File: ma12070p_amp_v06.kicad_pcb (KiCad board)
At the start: 2 copper layers, 100.4 x 80.4 mm, 83 parts, among them U1 MAX16956, U2 MA12070P

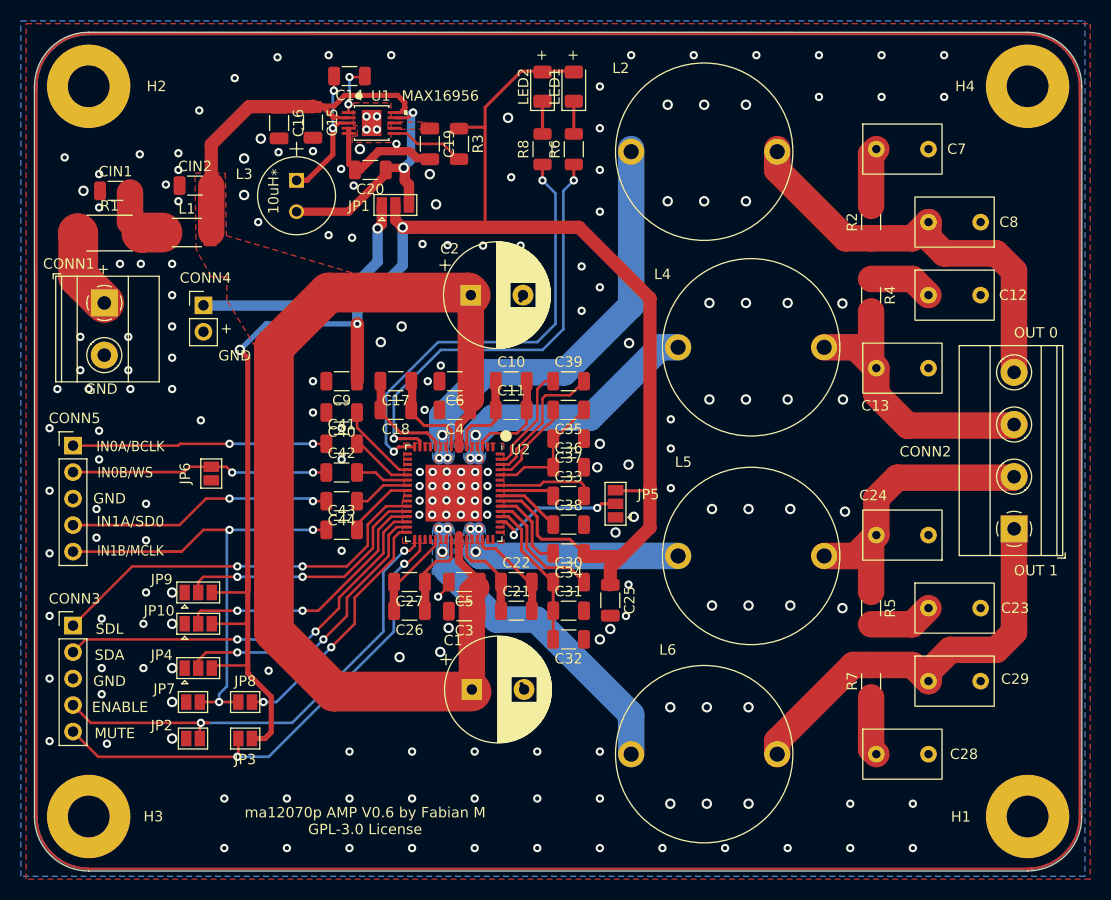
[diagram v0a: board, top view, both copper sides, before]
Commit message: redo of DRC because of mistake
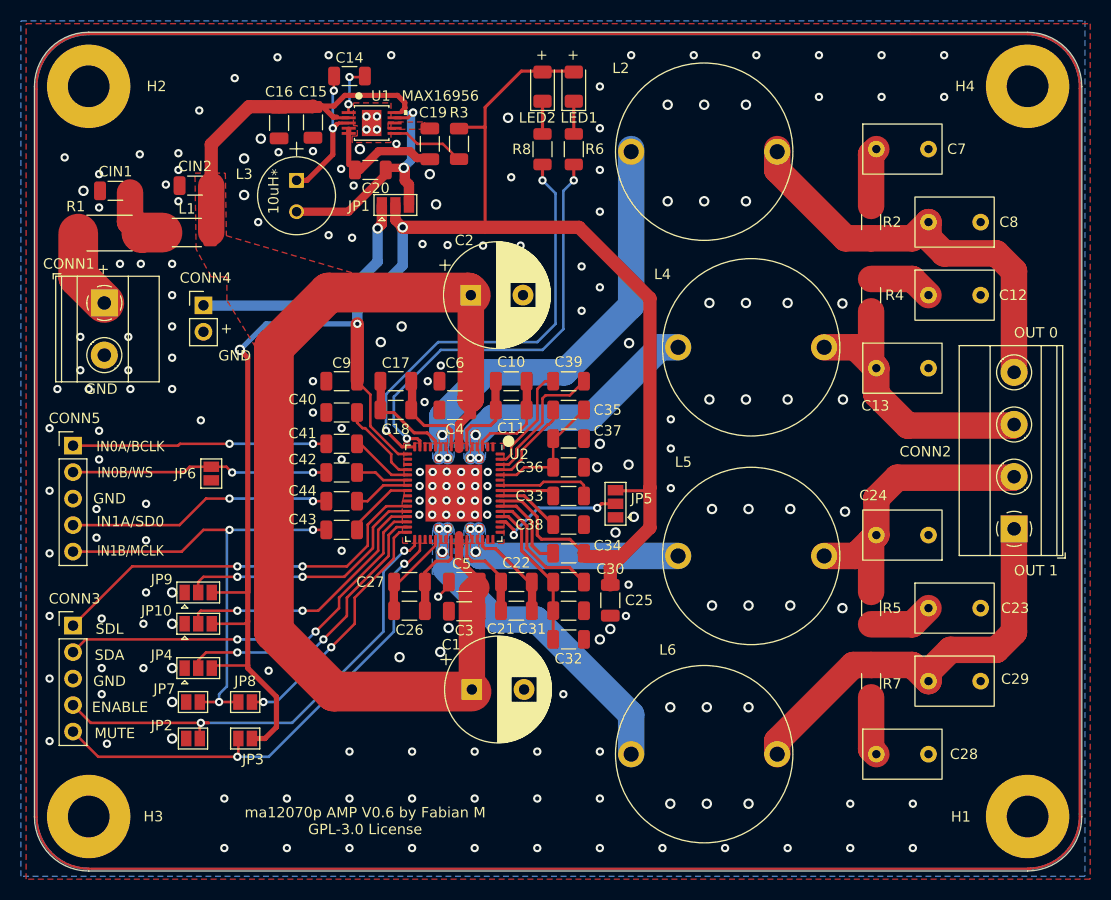
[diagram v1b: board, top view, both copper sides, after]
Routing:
- net VDD: track 185.7 -> 190.7 mm
- net Net-(C43-Pad1): track 47.7 -> 45.8 mm
- net ERR: track 42.3 -> 41.1 mm
- net Net-(C21-Pad1): track 9.75 -> 8.88 mm
- net CLIP: track 41.7 -> 41.0 mm

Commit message: added kicad logo to board
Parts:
- added REF**: logo, logo:logo, B.Cu at (145.4, 118.1)

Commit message: working on v0.7
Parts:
- added JP9: SolderJumper_3_Open, Jumper:SolderJumper-3_P1.3mm_Open_Pad1.0x1.5mm, F.Cu at (167.2, 87.8)
- JP1: footprint Jumper:SolderJumper-3_P1.3mm_Open_Pad1.0x1.5mm -> Connector_PinHeader_2.54mm:PinHeader_1x03_P2.54mm_Vertical
- JP10, JP4: value SolderJumper_3_Open -> Jumper:Jumper_3_Open; footprint Jumper:SolderJumper-3_P1.3mm_Open_Pad1.0x1.5mm -> Connector_PinHeader_2.54mm:PinHeader_1x03_P2.54mm_Vertical
- JP11: renamed from JP9; footprint Jumper:SolderJumper-3_P1.3mm_Open_Pad1.0x1.5mm -> Connector_PinHeader_2.54mm:PinHeader_1x03_P2.54mm_Vertical
- JP2, JP3, JP6, JP7, JP8: footprint Jumper:SolderJumper-2_P1.3mm_Open_Pad1.0x1.5mm -> Connector_PinHeader_2.54mm:PinHeader_1x02_P2.54mm_Vertical
- moved JP7 16.0 mm to (126.2, 92.0), turned to -90 degrees
- moved JP8 13.5 mm to (123.7, 96.0), turned to 90 degrees
- moved JP3 11.0 mm to (141.0, 111.5), turned to 90 degrees
- moved JP2 10.0 mm to (135.0, 111.5), turned to -90 degrees
- moved JP1 6.26 mm to (141.8, 66.0), turned to 180 degrees
- moved JP4 6.04 mm to (121.5, 109.2), turned to 90 degrees
- moved JP5 6.01 mm to (167.2, 83.2), turned to 0 degrees
- moved JP10 5.68 mm to (121.7, 104.8), turned to 90 degrees
- moved R3 5.49 mm to (147.8, 59.2), turned to 90 degrees
- moved JP11 4.67 mm to (121.7, 100.2), turned to 90 degrees
- moved JP6 1.72 mm to (126.3, 87.8), turned to -90 degrees
- moved C19 0.25 mm to (147.8, 54.2)
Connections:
- net Net-(C10-Pad1) renamed /CF0AP
- net Net-(C10-Pad2) renamed /CF0AN
- net Net-(C14-Pad1) renamed /BST
- net Net-(C14-Pad2) renamed /LX
- net Net-(C17-Pad1) renamed /CF0BP
- net Net-(C17-Pad2) renamed /CF0BN
- net Net-(C19-Pad1) renamed /BIAS/MODE
- net Net-(C21-Pad1) renamed /CF1AP
- net Net-(C21-Pad2) renamed /CF1AN
- net Net-(C26-Pad1) renamed /CF1BP
- net Net-(C26-Pad2) renamed /CF1BN
- net Net-(C30-Pad1) renamed /CGD1N
- net Net-(C30-Pad2) renamed /CGD1P
- net Net-(C33-Pad1) renamed /CFDCP
- net Net-(C33-Pad2) renamed /CFDCN
- net Net-(C34-Pad2) renamed /VGDC
- net Net-(C35-Pad1) renamed /CFD0P
- net Net-(C35-Pad2) renamed /CGDON
- net Net-(C38-Pad1) renamed /CDC
- net Net-(C39-Pad1) renamed /CFGDN
- net Net-(C39-Pad2) renamed /CFGDP
- net Net-(C40-Pad1) renamed /CREF
- net Net-(CIN1-Pad2) renamed /RCSUP
- net Net-(CONN1-Pad1) renamed /VSUP
- net Net-(R3-Pad2) renamed /NRST
- C41 pad 1: Net-(C41-Pad1) -> IN0A
- C42 pad 1: Net-(C42-Pad1) -> IN0B
- C43 pad 1: Net-(C43-Pad1) -> IN1B
- C44 pad 2: Net-(C44-Pad2) -> IN1A
- CONN5 pad 1: Net-(C41-Pad1) -> IN0A
- CONN5 pad 2: Net-(C42-Pad1) -> IN0B
- CONN5 pad 4: Net-(C44-Pad2) -> IN1A
- CONN5 pad 5: Net-(C43-Pad1) -> IN1B
- JP4 pad 3: VDD -> unconnected-(JP4-Pad3)
- JP6 pad 1: GND -> IN0B
- JP6 pad 2: Net-(C42-Pad1) -> GND
- JP7 pad 1: GND -> IN1B
- JP7 pad 2: Net-(C43-Pad1) -> GND
- JP8 pad 1: CLKIO -> IN1B
- JP8 pad 2: Net-(C43-Pad1) -> CLKIO
- U2 pad 50: GND -> MSEL1
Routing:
- net Net-(C43-Pad1): track 45.8 -> 0.00 mm, vias 3 -> 0
- net IN1B: track 6.71 -> 35.9 mm, vias 0 -> 1
- net IN0B: track 5.14 -> 30.9 mm, vias 0 -> 1
- net Net-(C44-Pad2): track 25.4 -> 0.00 mm, vias 2 -> 0
- net IN1A: track 5.47 -> 30.9 mm, vias 0 -> 2
- net Net-(C42-Pad1): track 24.7 -> 0.00 mm, vias 2 -> 0
- net Net-(C41-Pad1): track 24.3 -> 0.00 mm, vias 2 -> 0
- net IN0A: track 6.07 -> 30.4 mm, vias 0 -> 2
- net MSEL1: track 0.00 -> 15.9 mm, vias 0 -> 2
- net Ext_supply_5V: track 24.1 -> 17.4 mm, vias 1 -> 0
- net AD1: track 26.1 -> 31.1 mm, vias 2 -> 1
- net CLKMS: track 28.3 -> 33.0 mm, vias 2 -> 1
- net VDD: track 190.7 -> 186.2 mm, vias 3 -> 2
- net MUTE: track 48.5 -> 52.5 mm, vias 2 -> 1
- net MSEL0: track 13.3 -> 17.0 mm
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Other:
- board text added: "EN"
- board text removed: "ENABLE"

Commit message: changes
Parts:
- moved C15 3.25 mm to (133.2, 52.5)
- moved C16 3.25 mm to (136.5, 52.5)
- moved C31 2.75 mm to (161.0, 102.0)
- moved C32 2.75 mm to (161.0, 99.2)
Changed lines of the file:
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@@
   )
   (footprint "Capacitor_SMD:C_1206_3216Metric" (layer "F.Cu")
-    (at 133.25 52.5 -90)
+    (at 136.5 52.525 -90)
     (descr "Capacitor SMD 1206 (3216 Metric), square (rectangular) end terminal, IPC_7351 nominal, (Body size source: IPC-SM-782 page 76, https://www.pcb-3d.com/wordpress/wp-content/uploads/ipc-sm-782a_amendment_1_and_2.pdf), generated with kicad-footprint-generator")
     (tags "capacitor")
@@
   )
   (footprint "Capacitor_SMD:C_1206_3216Metric" (layer "F.Cu")
-    (at 136.5 52.4375 -90)
+    (at 133.25 52.5 -90)
     (descr "Capacitor SMD 1206 (3216 Metric), square (rectangular) end terminal, IPC_7351 nominal, (Body size source: IPC-SM-782 page 76, https://www.pcb-3d.com/wordpress/wp-content/uploads/ipc-sm-782a_amendment_1_and_2.pdf), generated with kicad-footprint-generator")
     (tags "capacitor")
@@
   )
   (footprint "Capacitor_SMD:C_1206_3216Metric" (layer "F.Cu")
-    (at 161 99.25)
+    (at 161 102)
     (descr "Capacitor SMD 1206 (3216 Metric), square (rectangular) end terminal, IPC_7351 nominal, (Body size source: IPC-SM-782 page 76, https://www.pcb-3d.com/wordpress/wp-content/uploads/ipc-sm-782a_amendment_1_and_2.pdf), generated with kicad-footprint-generator")
     (tags "capacitor")
@@
   )
   (footprint "Capacitor_SMD:C_1206_3216Metric" (layer "F.Cu")
-    (at 161 102 180)
-    (descr "Capacitor SMD 1206 (3216 Metric), square (rectangular) end terminal, IPC_7351 nominal, (Body size source: IPC-SM-782 page 76, https://www.pcb-3d.com/wordpress/wp-content/uploads/ipc-sm-782a_amendment_1_and_2.pdf), generated with kicad-footprint-generator")
-    (tags "capacitor")
+    (at 161 99.25 180)
+    (descr "Capacitor SMD 1206 (3216 Metric), square (rectangular) end terminal, IPC_7351 nominal, (Body size source: IPC-SM-782 page 76, https://www.pcb-3d.com/wordpress/wp-content/uploads/ipc-sm-782a_amendment_1_and_2.pdf), generated with kicad-footprint-generator")
+    (tags "capacitor")
